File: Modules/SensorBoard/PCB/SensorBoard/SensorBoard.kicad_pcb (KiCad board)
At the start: 2 copper layers, 45.7 x 52.1 mm, 9 parts, among them J2 PT100_Ext, J3 PT100_Int, J4 GPS, J5 PROG, J7 Micro_SD_Card_Det1, U2 BMI160, U3 BME280

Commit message: Finished Supply board
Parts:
- removed J5: PROG, Connector_PinHeader_2.54mm:PinHeader_1x04_P2.54mm_Vertical
- removed REF**: ESP32-WROOM-32UE, RF_Module:ESP32-WROOM-32UE
- removed U2: BMI160, Package_LGA:Bosch_LGA-14_3x2.5mm_P0.5mm
- added C12: 100nF, Capacitor_SMD:C_0603_1608Metric_Pad1.08x0.95mm_HandSolder, F.Cu at (152.2, 105.3)
- added C13: 100nF, Capacitor_SMD:C_0603_1608Metric_Pad1.08x0.95mm_HandSolder, F.Cu at (152.2, 103.7)
- added C14: 100nF, Capacitor_SMD:C_0603_1608Metric_Pad1.08x0.95mm_HandSolder, F.Cu at (155.1, 113.8)
- added C15: 100nF, Capacitor_SMD:C_0603_1608Metric_Pad1.08x0.95mm_HandSolder, F.Cu at (155.1, 115.3)
- added C2: 100nF, Capacitor_SMD:C_0603_1608Metric_Pad1.08x0.95mm_HandSolder, F.Cu at (198.1, 104.2)
- added J6: Micro_SD_Card, IcaroFootprints:microSD-Receptacle-SelfEject, B.Cu at (158.2, 126.3)
- added JP1: BOOT_SELECT, Connector_PinHeader_2.54mm:PinHeader_1x03_P2.54mm_Vertical, F.Cu at (152.2, 100.3)
- added JP2: BME280_Addr_Sel, Jumper:SolderJumper-3_P1.3mm_Open_RoundedPad1.0x1.5mm, F.Cu at (155.8, 107.8)
- added R10: 10k, Resistor_SMD:R_0603_1608Metric_Pad0.98x0.95mm_HandSolder, F.Cu at (192.1, 109.2)
- added R11: 10k, Resistor_SMD:R_0603_1608Metric_Pad0.98x0.95mm_HandSolder, F.Cu at (192.1, 117.4)
- added R12: 10k, Resistor_SMD:R_0603_1608Metric_Pad0.98x0.95mm_HandSolder, F.Cu at (192.1, 120.7)
- added R20: 10k, Resistor_SMD:R_0603_1608Metric_Pad0.98x0.95mm_HandSolder, F.Cu at (192.1, 124.0)
- added R7: 10k, Resistor_SMD:R_0603_1608Metric_Pad0.98x0.95mm_HandSolder, F.Cu at (192.1, 104.2)
- added R8: 10k, Resistor_SMD:R_0603_1608Metric_Pad0.98x0.95mm_HandSolder, F.Cu at (192.1, 107.5)
- added R9: 10k, Resistor_SMD:R_0603_1608Metric_Pad0.98x0.95mm_HandSolder, F.Cu at (192.1, 105.7)
- added U4: ESP32-WROOM-E, RF_Module:ESP32-WROOM-32UE, F.Cu at (172.4, 112.5)
- added U6: BMI160, Package_LGA:Bosch_LGA-14_3x2.5mm_P0.5mm, F.Cu at (158.6, 113.8)
- J4: footprint Connector_JST:JST_PH_S4B-PH-K_1x04_P2.00mm_Horizontal -> Connector_JST:JST_ZH_S6B-ZR-SM4A-TF_1x06-1MP_P1.50mm_Horizontal
- J7: value Micro_SD_Card_Det1 -> PROGRAMMING; footprint IcaroFootprints:microSD-Receptacle-SelfEject -> Connector_PinHeader_2.54mm:PinHeader_1x04_P2.54mm_Vertical
- moved J7 17.4 mm to (147.7, 112.3)
- moved U3 12.4 mm to (155.8, 104.4), turned to -90 degrees
- moved J4 2.99 mm to (179.4, 136.5)
- moved J1 1.44 mm to (163.3, 93.4)
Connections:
- J7 pad 1: unconnected-(J7-DAT2-Pad1) -> +3V3
- J7 pad 2: unconnected-(J7-DAT3/CD-Pad2) -> Net-(J7-Pin_2)
- J7 pad 3: unconnected-(J7-CMD-Pad3) -> Net-(J7-Pin_3)
- J7 pad 4: unconnected-(J7-VDD-Pad4) -> GND
- U3 pad 1: unconnected-(U3-GND-Pad1) -> GND
- U3 pad 2: unconnected-(U3-CSB-Pad2) -> +3V3
- U3 pad 3: unconnected-(U3-SDI-Pad3) -> /Microcontroller/I2C_BME.SDA
- U3 pad 4: unconnected-(U3-SCK-Pad4) -> /Microcontroller/I2C_BME.SCL
- U3 pad 5: unconnected-(U3-SDO-Pad5) -> Net-(JP2-C)
- U3 pad 6: unconnected-(U3-VDDIO-Pad6) -> +3V3
- U3 pad 7: unconnected-(U3-GND-Pad7) -> GND
- U3 pad 8: unconnected-(U3-VDD-Pad8) -> +3V3
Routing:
- net GND: track 0.00 -> 42.3 mm, vias 0 -> 5
- net +3V3: track 0.00 -> 28.0 mm
- net /Microcontroller/SPI_IMU.CS0: track 0.00 -> 25.2 mm, vias 0 -> 2
- net Net-(J7-Pin_2): track 0.00 -> 17.4 mm, vias 0 -> 1
- net Net-(J7-Pin_3): track 0.00 -> 16.2 mm, vias 0 -> 1
- net Net-(JP1-C): track 0.00 -> 10.6 mm
- net /Microcontroller/I2C_BME.SCL: track 0.00 -> 10.6 mm
- net /Microcontroller/I2C_BME.SDA: track 0.00 -> 10.3 mm
- net /Microcontroller/SPI_IMU.SCK: track 0.00 -> 8.43 mm
- net /Microcontroller/SPI_IMU.MOSI: track 0.00 -> 7.70 mm
- net /Microcontroller/SPI_IMU.MISO: track 0.00 -> 5.23 mm
- net Net-(JP2-C): track 0.00 -> 2.82 mm
- added copper zone on B.Cu, net GND
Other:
- board size 45.7 x 52.1 mm -> 50 x 60 mm

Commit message: Organizadas resistencias y condensador / Enrutado
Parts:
- moved R9 44.4 mm to (155.3, 130.5)
- moved R10 43.8 mm to (155.3, 133.0), turned to 180 degrees
- moved R11 34.9 mm to (159.8, 130.5)
- moved R12 34.6 mm to (159.8, 133.0), turned to 180 degrees
- moved R20 29.0 mm to (163.8, 130.5), turned to 180 degrees
- moved C2 18.4 mm to (184.8, 117.0), turned to 180 degrees
- moved R7 13.0 mm to (184.8, 115.0)
- moved R8 8.55 mm to (184.8, 112.0)
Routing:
- net +3V3: track 28.0 -> 178.3 mm, vias 0 -> 1
- net /Microcontroller/SD_DATA1: track 0.00 -> 68.9 mm, vias 0 -> 3
- net /Microcontroller/SD_DATA0: track 0.00 -> 63.0 mm, vias 0 -> 3
- net /Microcontroller/SD_DATA3: track 0.00 -> 55.5 mm, vias 0 -> 3
- net GND: track 42.3 -> 94.6 mm, vias 5 -> 6
- net /Microcontroller/SD_DATA2: track 0.00 -> 43.4 mm, vias 0 -> 1
- net /Microcontroller/SD_CMD: track 0.00 -> 37.2 mm, vias 0 -> 2
- net /Microcontroller/SD_CLK: track 0.00 -> 32.2 mm, vias 0 -> 2
- net Net-(U4-EN/CHIP_PU): track 0.00 -> 9.77 mm
- net /CD_DETECT: track 0.00 -> 6.32 mm, vias 0 -> 2
- removed copper zone on B.Cu, net GND

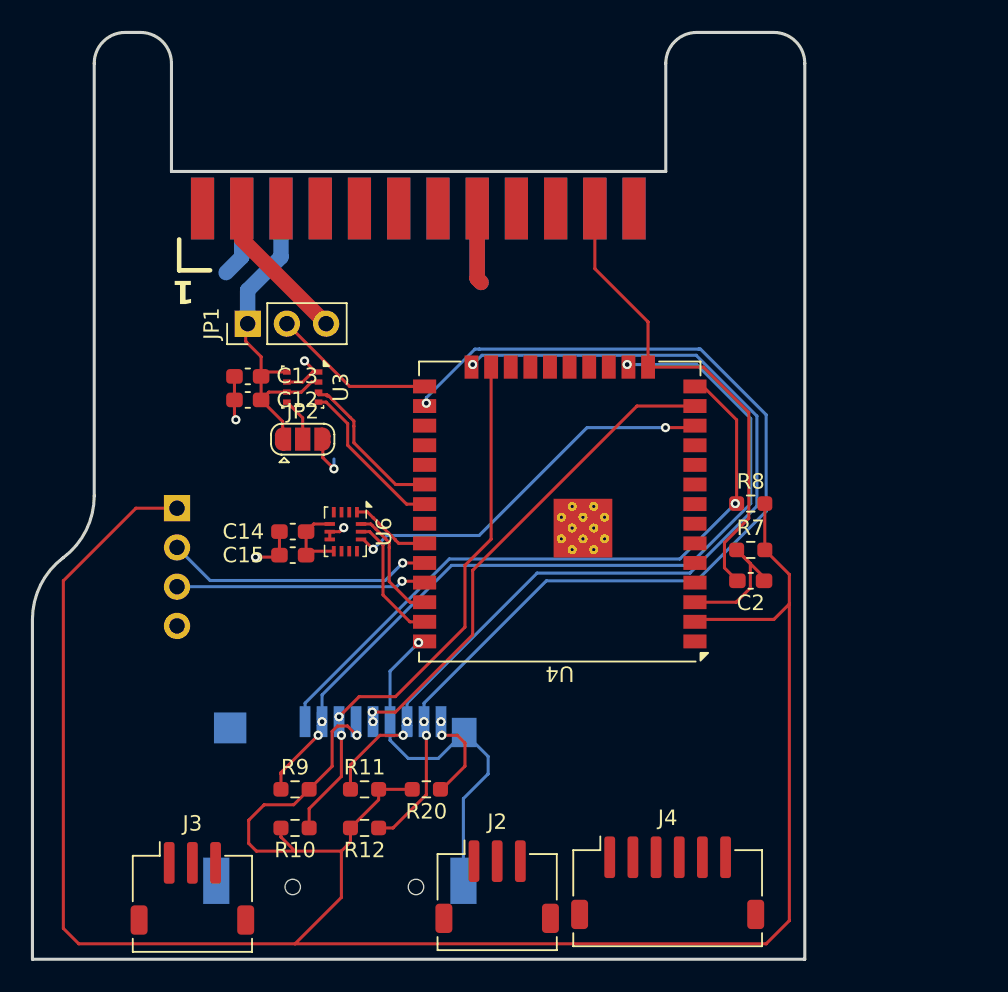
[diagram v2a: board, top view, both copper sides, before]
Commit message: Enrutado de diseño de PT100 en la sensorboard
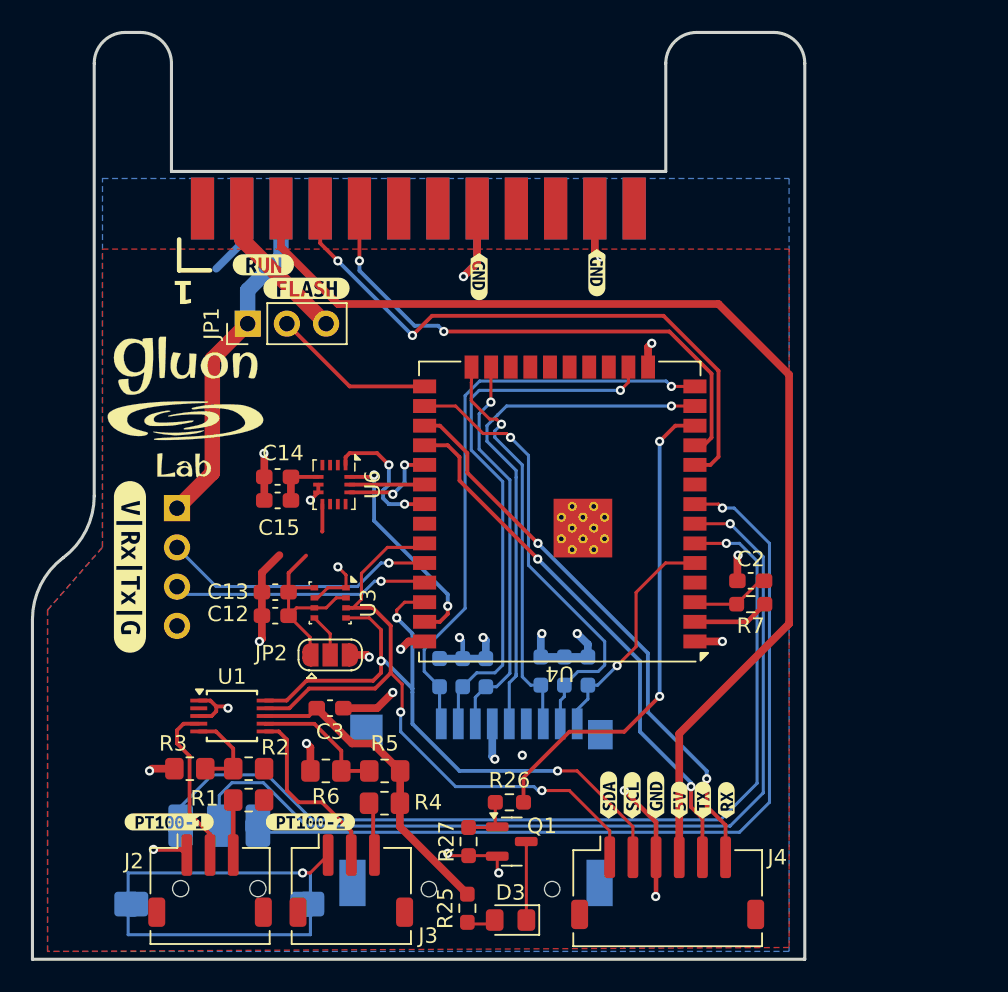
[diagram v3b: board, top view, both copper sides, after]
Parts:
- added C3: 100nF, Capacitor_SMD:C_0603_1608Metric_Pad1.08x0.95mm_HandSolder, F.Cu at (157.6, 125.2)
- added D3: LED, LED_SMD:LED_0805_2012Metric_Pad1.15x1.40mm_HandSolder, F.Cu at (169.2, 138.9)
- added G***: LOGO, IcaroFootprints:LogoGluon_12mm, F.Cu at (148.2, 105.4)
- added Q1: IRLM2502, Package_TO_SOT_SMD:SOT-23, F.Cu at (169.3, 133.8)
- added R1: 1k, Resistor_SMD:R_0805_2012Metric_Pad1.20x1.40mm_HandSolder, F.Cu at (152.3, 131.2)
- added R2: 1k, Resistor_SMD:R_0805_2012Metric_Pad1.20x1.40mm_HandSolder, F.Cu at (152.3, 129.1)
- added R25: 2k2, Resistor_SMD:R_0603_1608Metric_Pad0.98x0.95mm_HandSolder, F.Cu at (166.5, 138.2)
- added R26: 220, Resistor_SMD:R_0603_1608Metric_Pad0.98x0.95mm_HandSolder, F.Cu at (169.2, 131.3)
- added R27: 1Meg, Resistor_SMD:R_0603_1608Metric_Pad0.98x0.95mm_HandSolder, F.Cu at (166.5, 133.8)
- added R3: 68, Resistor_SMD:R_0805_2012Metric_Pad1.20x1.40mm_HandSolder, F.Cu at (148.5, 129.1)
- added R4: 1k, Resistor_SMD:R_0805_2012Metric_Pad1.20x1.40mm_HandSolder, F.Cu at (161.1, 131.4)
- added R5: 1k, Resistor_SMD:R_0805_2012Metric_Pad1.20x1.40mm_HandSolder, F.Cu at (161.1, 129.3)
- added R6: 68, Resistor_SMD:R_0805_2012Metric_Pad1.20x1.40mm_HandSolder, F.Cu at (157.3, 129.3)
- added U1: ADS1115IDGS, Package_SO:TSSOP-10_3x3mm_P0.5mm, F.Cu at (151.2, 125.7)
- added U2: ~, IcaroFootprints:WheelSwitch, B.Cu at (150.4, 136.9)
- added kibuzzard-67C3A99D: G***, kibuzzard-67C3A99D, F.Cu at (144.6, 116.1)
- added kibuzzard-67C3A9D6: G***, kibuzzard-67C3A9D6, F.Cu at (147.1, 132.6)
- added kibuzzard-67C3AA69: G***, kibuzzard-67C3AA69, F.Cu at (156.3, 132.6)
- added kibuzzard-67C3AA71: G***, kibuzzard-67C3AA71, F.Cu at (175.6, 130.8)
- added kibuzzard-67C3AA85: G***, kibuzzard-67C3AA85, F.Cu at (177.1, 130.9)
- added kibuzzard-67C3AAB2: G***, kibuzzard-67C3AAB2, F.Cu at (167.2, 97.3)
- added kibuzzard-67C3AAB2: G***, kibuzzard-67C3AAB2, F.Cu at (178.6, 130.8)
- added kibuzzard-67C3AAB2: G***, kibuzzard-67C3AAB2, F.Cu at (174.8, 97.0)
- added kibuzzard-67C3AAB2: G***, kibuzzard-67C3AAB2, B.Cu at (167.2, 97.3)
- added kibuzzard-67C3AAB2: G***, kibuzzard-67C3AAB2, B.Cu at (174.8, 97.0)
- added kibuzzard-67C3AAB2: G***, kibuzzard-67C3AAB2, B.Cu at (152.0, 97.3)
- added kibuzzard-67C3AABB: G***, kibuzzard-67C3AABB, F.Cu at (180.2, 131.2)
- added kibuzzard-67C3AAC1: G***, kibuzzard-67C3AAC1, F.Cu at (181.7, 131.2)
- added kibuzzard-67C3AAC6: G***, kibuzzard-67C3AAC6, F.Cu at (183.2, 131.2)
- added kibuzzard-67C3AB9B: G***, kibuzzard-67C3AB9B, F.Cu at (153.2, 96.5)
- added kibuzzard-67C3AC34: G***, kibuzzard-67C3AC34, B.Cu at (154.3, 97.3)
- added kibuzzard-67C4846B: G***, kibuzzard-67C4846B, F.Cu at (156.0, 98.0)
- J2: value PT100_Ext -> PT100_1
- J3: value PT100_Int -> PT100_2
- J4: value GPS -> Conn_01x06
- R10, R11, R12, R20, R8, R9: moved to B.Cu
- moved R8 22.9 mm to (164.7, 122.9), turned to 90 degrees
- moved J2 18.6 mm to (149.8, 136.4)
- moved R12 16.4 mm to (172.7, 122.8), turned to 90 degrees
- moved R10 15.9 mm to (167.6, 122.9), turned to 90 degrees
- moved C12 14.1 mm to (154.0, 119.2)
- moved C13 14.1 mm to (154.0, 117.7)
- moved JP2 14.1 mm to (157.6, 121.8)
- moved U3 14.1 mm to (157.6, 118.4)
- moved R11 13.7 mm to (171.2, 122.8), turned to 90 degrees
- moved R9 13.2 mm to (166.2, 122.9), turned to 90 degrees
- moved R20 13.0 mm to (174.3, 122.8), turned to 90 degrees
- moved J3 10.3 mm to (158.9, 136.4)
- moved J6 8.82 mm to (167.0, 126.4)
- moved C14 3.67 mm to (154.2, 110.2)
- moved C15 3.67 mm to (154.2, 111.8)
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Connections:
- net Net-(J7-Pin_2) renamed /Microcontroller/UART_RX
- net Net-(J7-Pin_3) renamed /Microcontroller/UART_TX
- J1 pad 7: unconnected-(J1-SDA_0-Pad7) -> /Microcontroller/I2C_EXT.SDA
- J1 pad 9: unconnected-(J1-SCL_0-Pad9) -> /Microcontroller/I2C_EXT.SCL
- J2 pad 1: unconnected-(J2-Pin_1-Pad1) -> GND
- J2 pad 2: unconnected-(J2-Pin_2-Pad2) -> /PT100/PT100_1_P
- J2 pad 3: unconnected-(J2-Pin_3-Pad3) -> Net-(J2-Pin_3)
- J3 pad 1: unconnected-(J3-Pin_1-Pad1) -> GND
- J3 pad 2: unconnected-(J3-Pin_2-Pad2) -> /PT100/PT100_2_P
- J3 pad 3: unconnected-(J3-Pin_3-Pad3) -> Net-(J3-Pin_3)
- J4 pad 1: unconnected-(J4-Pin_1-Pad1) -> /Microcontroller/I2C_INT.SDA
- J4 pad 2: unconnected-(J4-Pin_2-Pad2) -> /Microcontroller/I2C_INT.SCL
- J4 pad 3: unconnected-(J4-Pin_3-Pad3) -> GND
- J4 pad 4: unconnected-(J4-Pin_4-Pad4) -> +5V
- J4 pad 5: (no net) -> /Microcontroller/UART_GPS.TX
- J4 pad 6: (no net) -> /Microcontroller/UART_GPS.RX
- J6 pad 9: /CD_DETECT -> /Microcontroller/CD_DETECT
- JP1 pad 2: Net-(JP1-C) -> unconnected-(JP1-C-Pad2)
- R20 pad 1: /CD_DETECT -> /Microcontroller/CD_DETECT
- U3 pad 3: /Microcontroller/I2C_BME.SDA -> /Microcontroller/I2C_INT.SDA
- U3 pad 4: /Microcontroller/I2C_BME.SCL -> /Microcontroller/I2C_INT.SCL
- U4 pad 10: unconnected-(U4-DAC_1/ADC2_CH8/GPIO25-Pad10) -> /Microcontroller/I2C_EXT.SDA
- U4 pad 11: unconnected-(U4-DAC_2/ADC2_CH9/GPIO26-Pad11) -> /Microcontroller/I2C_EXT.SCL
- U4 pad 12: /Microcontroller/SPI_IMU.CS0 -> /Microcontroller/LED_PIN
- U4 pad 25: Net-(JP1-C) -> unconnected-(U4-GPIO0/BOOT/ADC2_CH1-Pad25)
- U4 pad 27: UART_GPS.RX -> /Microcontroller/UART_GPS.RX
- U4 pad 28: UART_GPS.TX -> /Microcontroller/UART_GPS.TX
- U4 pad 29: unconnected-(U4-GPIO5-Pad29) -> /Microcontroller/SPI_IMU.CS0
- U4 pad 30: /Microcontroller/I2C_BME.SDA -> /Microcontroller/SPI_IMU.SCK
- U4 pad 31: /Microcontroller/I2C_BME.SCL -> /Microcontroller/SPI_IMU.MISO
- U4 pad 33: /Microcontroller/SPI_IMU.MISO -> /Microcontroller/I2C_INT.SDA
- U4 pad 36: /Microcontroller/SPI_IMU.MOSI -> /Microcontroller/I2C_INT.SCL
- U4 pad 37: /Microcontroller/SPI_IMU.SCK -> /Microcontroller/SPI_IMU.MOSI
- U4 pad 5: unconnected-(U4-SENSOR_VN/GPIO39/ADC1_CH3-Pad5) -> /Microcontroller/CD_DETECT
- U4 pad 6: unconnected-(U4-GPIO34/ADC1_CH6-Pad6) -> Net-(U2-L)
- U4 pad 7: unconnected-(U4-GPIO35/ADC1_CH7-Pad7) -> Net-(U2-Push)
- U4 pad 8: unconnected-(U4-32K_XP/GPIO32/ADC1_CH4-Pad8) -> Net-(U2-R)
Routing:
- net +3V3: track 178.3 -> 80.8 mm, vias 1 -> 5
- net +5V: track 0.00 -> 73.0 mm
- net Net-(U2-L): track 0.00 -> 60.1 mm, vias 0 -> 1
- net Net-(U2-Push): track 0.00 -> 59.7 mm, vias 0 -> 1
- net Net-(U2-R): track 0.00 -> 56.6 mm, vias 0 -> 1
- net /Microcontroller/I2C_INT.SDA: track 0.00 -> 45.4 mm, vias 0 -> 2
- net /Microcontroller/I2C_INT.SCL: track 0.00 -> 45.2 mm, vias 0 -> 3
- net /Microcontroller/I2C_EXT.SDA: track 0.00 -> 39.8 mm, vias 0 -> 2
- net /Microcontroller/SD_DATA1: track 68.9 -> 29.4 mm, vias 3 -> 1
- net /Microcontroller/SD_DATA0: track 63.0 -> 25.8 mm, vias 3 -> 1
- net /Microcontroller/UART_GPS.RX: track 0.00 -> 36.6 mm, vias 0 -> 2
- net /Microcontroller/UART_GPS.TX: track 0.00 -> 35.0 mm, vias 0 -> 2
- net /Microcontroller/I2C_EXT.SCL: track 0.00 -> 35.0 mm, vias 0 -> 2
- net /Microcontroller/LED_PIN: track 0.00 -> 31.8 mm, vias 0 -> 2
- net /Microcontroller/SD_DATA3: track 55.5 -> 35.4 mm, vias 3 -> 1
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- added copper zone on F.Cu, net +3V3
- added copper zone on B.Cu, net GND

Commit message: Finished Sensor and Backplane boards
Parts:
- added ?: , , F.Cu at (183.7, 86.1)
- added R13: 10k, Resistor_SMD:R_0603_1608Metric_Pad0.98x0.95mm_HandSolder, F.Cu at (159.6, 104.4)
- added R14: 10k, Resistor_SMD:R_0603_1608Metric_Pad0.98x0.95mm_HandSolder, F.Cu at (161.1, 104.4)
- added R15: 10k, Resistor_SMD:R_0603_1608Metric_Pad0.98x0.95mm_HandSolder, F.Cu at (163.8, 127.1)
- added R16: 10k, Resistor_SMD:R_0603_1608Metric_Pad0.98x0.95mm_HandSolder, F.Cu at (165.3, 127.1)
- added REF**: KiCad-Logo2_5mm_SilkScreen, Symbol:KiCad-Logo2_5mm_SilkScreen, B.Cu at (183.7, 98.0)
- added kibuzzard-67C81440: G***, kibuzzard-67C81440, F.Cu at (160.5, 99.3)
- moved U2 0.61 mm to (149.8, 136.8)
- moved J3 0.53 mm to (158.9, 136.9)
- moved J2 0.25 mm to (149.8, 136.6)
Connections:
- C2 pad 1: Net-(U4-EN/CHIP_PU) -> Net-(U2-L)
- JP1 pad 2: unconnected-(JP1-C-Pad2) -> Net-(JP1-C)
- R7 pad 1: Net-(U4-EN/CHIP_PU) -> Net-(U2-L)
- U4 pad 25: unconnected-(U4-GPIO0/BOOT/ADC2_CH1-Pad25) -> Net-(JP1-C)
- U4 pad 3: Net-(U4-EN/CHIP_PU) -> Net-(U2-L)
- U4 pad 6: Net-(U2-L) -> unconnected-(U4-GPIO34/ADC1_CH6-Pad6)
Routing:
- net Net-(JP1-C): track 0.00 -> 10.6 mm
- net (no net): track 10.6 -> 0.00 mm
- net Net-(U4-EN/CHIP_PU): track 5.15 -> 0.00 mm
- net /Microcontroller/I2C_EXT.SCL: track 35.0 -> 40.0 mm
- net /Microcontroller/I2C_INT.SCL: track 45.2 -> 49.3 mm, vias 3 -> 4
- net /Microcontroller/I2C_EXT.SDA: track 39.8 -> 43.7 mm
- net Net-(U2-L): track 60.1 -> 63.2 mm
- net /Microcontroller/I2C_INT.SDA: track 45.4 -> 47.3 mm
- net Net-(U2-Push): track 59.7 -> 60.3 mm
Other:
- board text added: "Proyecto Ícaro SensorBoard V1.0 by: @labgluon"
